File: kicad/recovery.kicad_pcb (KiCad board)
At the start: 2 copper layers, 84.1 x 61.7 mm, 50 parts, among them J1 Bus_PCI_Express_x1, J2 wago 2060-452/998-404, J3 wago 2060-452/998-404, J4 Conn_01x04, J5 Conn_01x02_Pin, J6 USB_C_Receptacle_USB2.0_16P, Q1 SI7232DN-T1-GE3, U2 RP2040, U4 W25Q128JVP, U9 MCP25625T-E/ML, X1 RP2040 Crystal, Y2 X322516MLB4SI

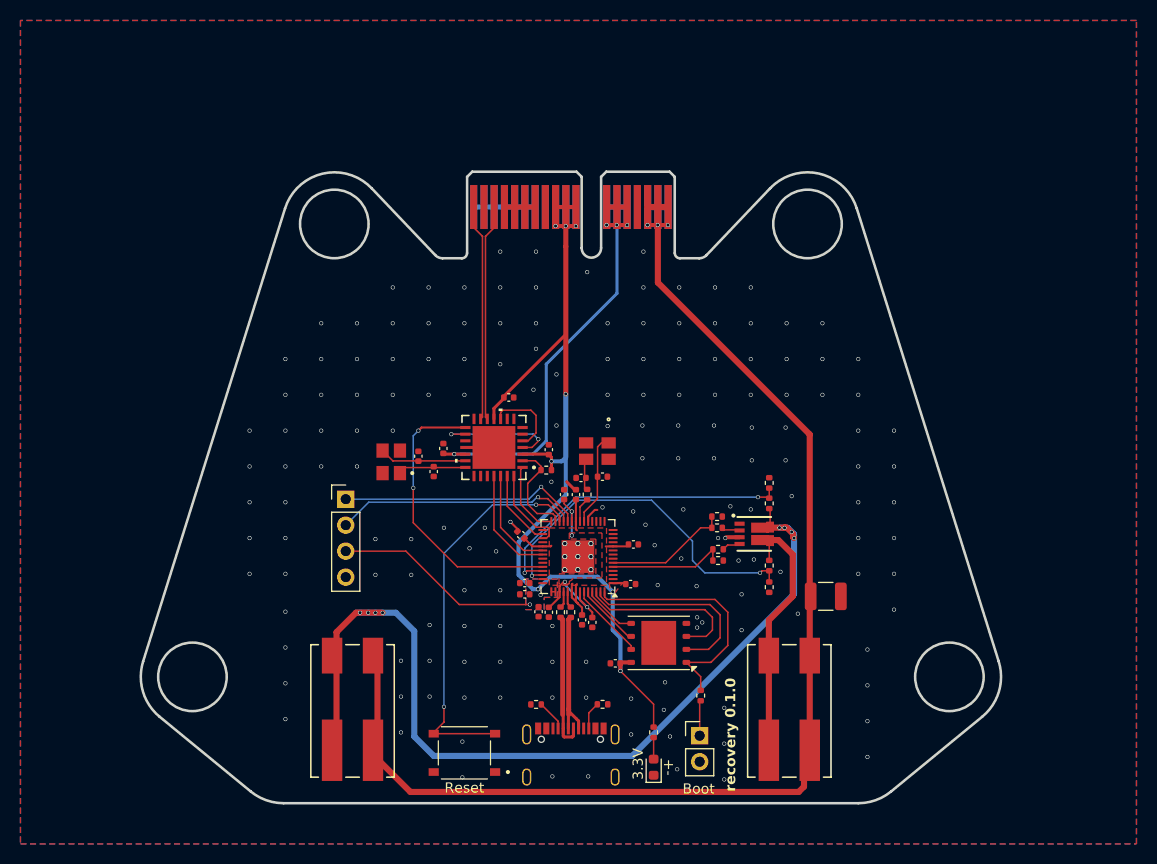
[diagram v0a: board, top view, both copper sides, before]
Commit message: feat: overhauled recovery board: added servos, solenoids, PWM-level shifters and firing circuit to layout
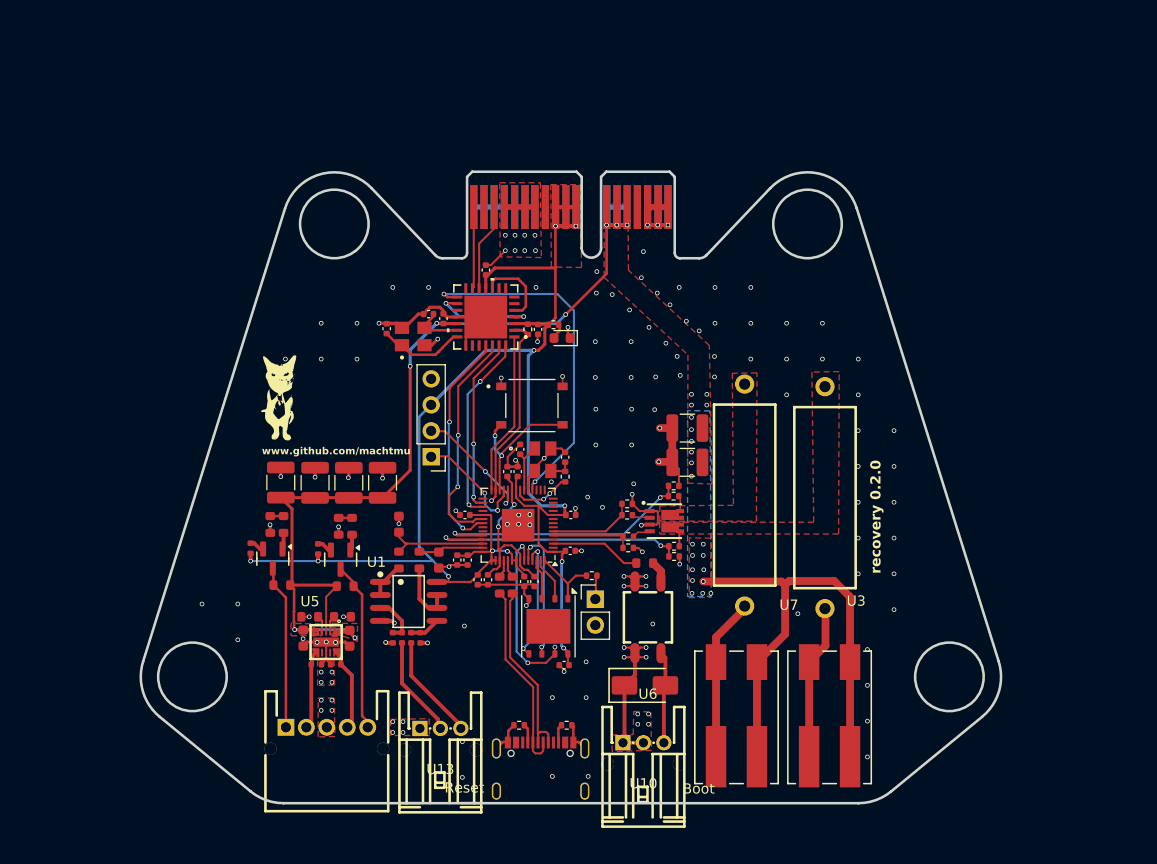
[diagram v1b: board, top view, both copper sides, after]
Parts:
- removed R203, R204: 27, Resistor_SMD:R_0402_1005Metric
- added C2: 100pF, PCM_JLCPCB:C_0603, F.Cu at (133.5, 98.7)
- added C21: 1uF, PCM_JLCPCB:C_0603, F.Cu at (120.2, 106.3)
- added C28: 1uF, PCM_JLCPCB:C_0603, F.Cu at (124.8, 106.3)
- added C29: 100nF, PCM_JLCPCB:C_0402, F.Cu at (123.4, 108.8)
- added C3: 100u, Capacitor_SMD:C_1210_3225Metric, F.Cu at (157.8, 89.1)
- added C30: 100nF, PCM_JLCPCB:C_0402, F.Cu at (121.5, 108.8)
- added C4: 100pF, PCM_JLCPCB:C_0603, F.Cu at (129.6, 95.2)
- added C5: 100u, Capacitor_SMD:C_1210_3225Metric, F.Cu at (118.0, 91.1)
- added C6: 100u, Capacitor_SMD:C_1210_3225Metric, F.Cu at (121.4, 91.1)
- added C7: 100u, Capacitor_SMD:C_1210_3225Metric, F.Cu at (128.0, 91.1)
- added C8: 100u, Capacitor_SMD:C_1210_3225Metric, F.Cu at (124.7, 91.1)
- added D2: SS210, PCM_JLCPCB:D_SMA, F.Cu at (153.7, 110.9)
- added G***: LOGO, LOGO, F.Cu at (117.8, 82.8)
- added Q2: AO3400A, PCM_JLCPCB:Q_SOT-23, F.Cu at (123.9, 98.6)
- added Q3: AO3400A, PCM_JLCPCB:Q_SOT-23, F.Cu at (117.3, 98.5)
- added R1: 100Ω, PCM_JLCPCB:R_0603, F.Cu at (131.6, 98.7)
- added R10: 300Ω, PCM_JLCPCB:R_0603, F.Cu at (153.6, 99.0)
- added R11: 27Ω, PCM_JLCPCB:R_0603, F.Cu at (139.4, 101.1)
- added R13: 5.1kΩ, PCM_JLCPCB:R_0603, F.Cu at (124.1, 104.2)
- added R14: 5.1kΩ, PCM_JLCPCB:R_0603, F.Cu at (120.9, 104.2)
- added R15: 120Ω, PCM_JLCPCB:R_0603, F.Cu at (125.0, 95.3)
- added R16: 5.1kΩ, PCM_JLCPCB:R_0603, F.Cu at (123.7, 95.3)
- added R17: 5.1kΩ, PCM_JLCPCB:R_0603, F.Cu at (117.0, 95.2)
- added R18: 120Ω, PCM_JLCPCB:R_0603, F.Cu at (118.3, 95.2)
- added R19: 5.1kΩ, PCM_JLCPCB:R_0603, F.Cu at (118.2, 101.1)
- added R24: 5.1kΩ, PCM_JLCPCB:R_0603, F.Cu at (124.3, 101.2)
- added R25: 10kΩ, PCM_JLCPCB:R_0402, F.Cu at (121.7, 97.6)
- added R26: 10kΩ, PCM_JLCPCB:R_0402, F.Cu at (115.1, 97.5)
- added R35: 27Ω, PCM_JLCPCB:R_0603, F.Cu at (140.7, 101.1)
- added R36: 100Ω, PCM_JLCPCB:R_0603, F.Cu at (129.6, 98.7)
- added R5: 100kΩ, PCM_JLCPCB:R_0402, F.Cu at (129.9, 106.2)
- added R6: 33kΩ, PCM_JLCPCB:R_0402, F.Cu at (129.0, 106.2)
- added R7: 100kΩ, PCM_JLCPCB:R_0402, F.Cu at (130.8, 106.2)
- added R8: 33kΩ, PCM_JLCPCB:R_0402, F.Cu at (131.7, 106.2)
- added U1: MCP6002T-I/SN, easyeda2kicad:SOIC-8_L4.9-W3.9-P1.27-LS6.0-BL, F.Cu at (130.6, 102.7)
- added U10: S03B-PASK-2, easyeda2kicad:CONN-TH_S03B-PASK-2-LF-SN, F.Cu at (153.5, 116.5)
- added U13: S03B-PASK-2, easyeda2kicad:CONN-TH_S03B-PASK-2-LF-SN, F.Cu at (133.7, 115.1)
- added U3: MOF5WS-5.1Ω±5% T, easyeda2kicad:RES-TH_BD6.0-L17.5-P21.50-D0.7, F.Cu at (171.2, 92.5)
- added U5: TPS22976DPUR, easyeda2kicad:WSON-14_L3.0-W2.0-P0.40-BL-EP-1, F.Cu at (122.5, 106.7)
- added U6: GAQY252G3S, easyeda2kicad:SOP-4_L4.3-W4.4-P2.54-LS7.0-BL, F.Cu at (153.9, 104.2)
- added U7: MOF5WS-5.1Ω±5% T, easyeda2kicad:RES-TH_BD6.0-L17.5-P21.50-D0.7, F.Cu at (163.4, 92.3)
- added U8: S05B-PASK-2(LF)(SN), easyeda2kicad:CONN-TH_S05B-PASK-2-LF-SN, F.Cu at (122.5, 115.0)
- moved D1 42.9 mm to (145.6, 77.0), turned to 180 degrees
- moved R2 41.0 mm to (144.7, 75.7), turned to 0 degrees
- moved J2 37.5 mm to (162.6, 114.0)
- moved S2 34.6 mm to (142.6, 83.5), turned to 0 degrees
- moved C1 21.3 mm to (157.8, 85.8), turned to 180 degrees
- moved J5 16.8 mm to (148.8, 102.5)
- moved R30 15.8 mm to (148.4, 100.2), turned to 0 degrees
- moved C94 14.7 mm to (128.4, 76.0), turned to 90 degrees
- moved C95 13.9 mm to (132.5, 74.6), turned to 180 degrees
- moved R91 13.9 mm to (142.2, 76.1), turned to -90 degrees
- moved U9 12.8 mm to (138.1, 74.9)
- moved C93 12.7 mm to (133.9, 75.0)
- moved C90 12.7 mm to (138.1, 70.3), turned to 90 degrees
- moved Y2 12.4 mm to (131.0, 76.8), turned to 90 degrees
- moved C92 11.8 mm to (143.2, 76.1), turned to -90 degrees
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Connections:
- C1 pad 1: v_lipo -> +5V
- J2 pad 3: v_lipo -> +5V
- J2 pad 4: v_lipo -> +5V
- J3 pad 3: v_lipo -> +5V
- J3 pad 4: v_lipo -> +5V
- J4 pad 1: /SWCLK -> /SWD
- J4 pad 2: /SWD -> /SWCLK
- Q1 pad 5: Net-(J3-1_1) -> Net-(Q1-Pad5)
- Q1 pad 6: Net-(J3-1_1) -> Net-(Q1-Pad5)
- Q1 pad 7: Net-(J2-1_1) -> Net-(Q1-Pad7)
- Q1 pad 8: Net-(J2-1_1) -> Net-(Q1-Pad7)
- R22 pad 2: Net-(J3-1_1) -> Net-(Q1-Pad5)
- R32 pad 2: Net-(J2-1_1) -> Net-(Q1-Pad7)
- U2 pad 18: unconnected-(U2-GPIO15-Pad18) -> CANSTBY
- U2 pad 3: unconnected-(U2-GPIO1-Pad3) -> /MCU_SOLENOID
- U2 pad 38: CANSTBY -> sense_m
- U2 pad 39: sense_m -> sense_d
- U2 pad 40: sense_d -> /PT_1
- U2 pad 41: unconnected-(U2-GPIO29_ADC3-Pad41) -> /PT_2
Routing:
- net v_lipo: track 119.1 -> 6.00 mm
- net GND: track 17.7 -> 122.7 mm, vias 178 -> 152
- net +5V: track 43.2 -> 141.3 mm, vias 4 -> 29
- net Net-(J2-1_1): track 92.3 -> 15.9 mm, vias 8 -> 0
- net /RUN: track 38.3 -> 14.4 mm
- net +3.3V: track 132.6 -> 151.7 mm, vias 10 -> 11
- net /5V_PWM1: track 0.00 -> 16.7 mm
- net /5V_PWM2: track 0.00 -> 16.2 mm
- net /QSPI_SS: track 24.5 -> 8.31 mm
- net /QSPI_SD1: track 18.9 -> 4.32 mm
- net CANH: track 21.1 -> 8.01 mm
- net /SWD: track 23.8 -> 11.1 mm, vias 1 -> 2
- net /QSPI_SD2: track 16.7 -> 3.96 mm
- net CANL: track 21.1 -> 8.57 mm
- net /SWCLK: track 24.0 -> 11.9 mm, vias 1 -> 2
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- added copper zone on B.Cu, net +5V
- added copper zone on F.Cu, net +5V
- added copper zone on In1.Cu, net GND
- added copper zone on In2.Cu, net GND
- added copper zone on F.Cu, net Net-(Q1-Pad5)
- added copper zone on F.Cu, net Net-(Q1-Pad7)
- removed copper zone on F.Cu, net +1V1
- removed copper zone on B.Cu, net +3.3V
- removed copper zone on B.Cu, net GND
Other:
- copper layers 2 -> 4
- board text added: "recovery 0.2.0"
- board text added: "www.github.com/machtmu"
- board text removed: "+-"
- board text removed: "3.3V"
- board text removed: "recovery 0.1.0"

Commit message: Feat: Completed layout, modified divider network for 5V PT operation
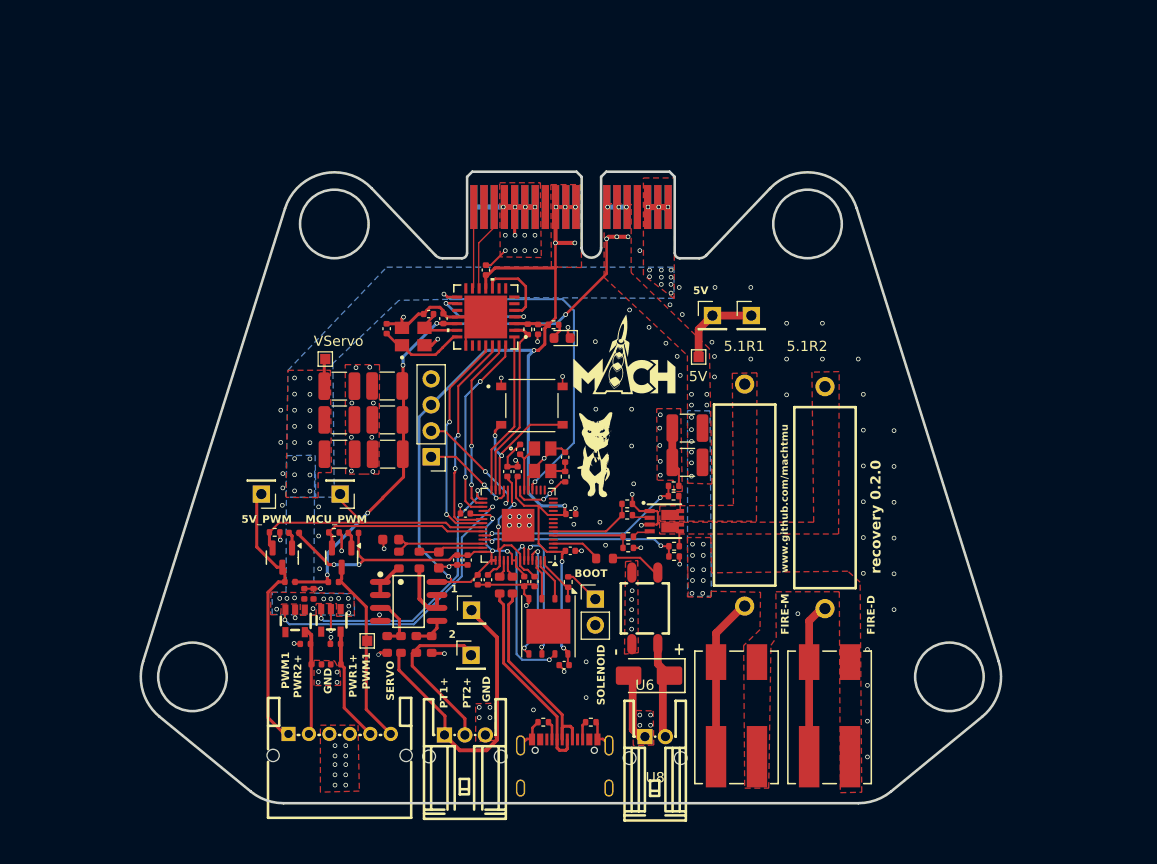
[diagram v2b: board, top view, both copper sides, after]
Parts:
- removed C21, C28: 1uF, PCM_JLCPCB:C_0603
- removed R19, R24: 5.1kΩ, PCM_JLCPCB:R_0603
- removed R25: 10kΩ, PCM_JLCPCB:R_0402
- removed R6, R8: 33kΩ, PCM_JLCPCB:R_0402
- removed U10: S03B-PASK-2, easyeda2kicad:CONN-TH_S03B-PASK-2-LF-SN
- added 5V: TestPoint_Pad_1.0x1.0mm, TestPoint:TestPoint_Pad_1.0x1.0mm, F.Cu at (158.9, 78.8)
- added C12: 100u, Capacitor_SMD:C_1210_3225Metric, F.Cu at (123.8, 85.0)
- added C12: 100u, Capacitor_SMD:C_1210_3225Metric, F.Cu at (123.8, 88.3)
- added C13: 100u, Capacitor_SMD:C_1210_3225Metric, F.Cu at (123.8, 81.7)
- added C5: 1uF, PCM_JLCPCB:C_0402, F.Cu at (120.3, 102.0)
- added C5: 100u, Capacitor_SMD:C_1210_3225Metric, F.Cu at (128.5, 88.3)
- added C6: 1uF, PCM_JLCPCB:C_0402, F.Cu at (121.2, 102.0)
- added CN1: S06B-PASK-2(LF)(SN), easyeda2kicad:CONN-TH_6P-P2.00_S06B-PASK-2-LF-SN, F.Cu at (123.8, 115.7)
- added G***: LOGO, LOGO, F.Cu at (151.7, 79.5)
- added PWM1: TestPoint_Pad_1.0x1.0mm, TestPoint:TestPoint_Pad_1.0x1.0mm, F.Cu at (126.5, 106.5)
- added R9: 10kΩ, PCM_JLCPCB:R_0402, F.Cu at (125.2, 96.0)
- added REF**: PinHeader_1x01_P2.54mm_Vertical, Connector_PinHeader_2.54mm:PinHeader_1x01_P2.54mm_Vertical, F.Cu at (164.1, 74.8)
- added REF**: PinHeader_1x01_P2.54mm_Vertical, Connector_PinHeader_2.54mm:PinHeader_1x01_P2.54mm_Vertical, F.Cu at (136.7, 103.5)
- added REF**: PinHeader_1x01_P2.54mm_Vertical, Connector_PinHeader_2.54mm:PinHeader_1x01_P2.54mm_Vertical, F.Cu at (160.2, 74.8)
- added REF**: PinHeader_1x01_P2.54mm_Vertical, Connector_PinHeader_2.54mm:PinHeader_1x01_P2.54mm_Vertical, F.Cu at (123.8, 92.2)
- added REF**: PinHeader_1x01_P2.54mm_Vertical, Connector_PinHeader_2.54mm:PinHeader_1x01_P2.54mm_Vertical, F.Cu at (136.7, 108.0)
- added REF**: PinHeader_1x01_P2.54mm_Vertical, Connector_PinHeader_2.54mm:PinHeader_1x01_P2.54mm_Vertical, F.Cu at (116.2, 92.2)
- added U11: TMI6240, easyeda2kicad:SOT-23-5_L2.9-W1.6-P0.95-LS2.8-BL, F.Cu at (123.0, 104.5)
- added VServo: TestPoint_Pad_1.0x1.0mm, TestPoint:TestPoint_Pad_1.0x1.0mm, F.Cu at (122.4, 79.0)
- C7, C8: value 100u -> 1uF; footprint Capacitor_SMD:C_1210_3225Metric -> PCM_JLCPCB:C_0402
- R13, R14: value 5.1kΩ -> 10kΩ; footprint PCM_JLCPCB:R_0603 -> PCM_JLCPCB:R_0402
- R15: value 120Ω -> 1k; footprint PCM_JLCPCB:R_0603 -> Resistor_SMD:R_0402_1005Metric
- R16: value 5.1kΩ -> 1k; footprint PCM_JLCPCB:R_0603 -> Resistor_SMD:R_0402_1005Metric
- R17: value 5.1kΩ -> 33kΩ
- R18: value 120Ω -> 100kΩ
- R5, R7: value 100kΩ -> 51kΩ; footprint PCM_JLCPCB:R_0402 -> PCM_JLCPCB:R_0603
- U5: value TPS22976DPUR -> TMI6240; footprint easyeda2kicad:WSON-14_L3.0-W2.0-P0.40-BL-EP-1 -> easyeda2kicad:SOT-23-5_L2.9-W1.6-P0.95-LS2.8-BL
- U8: value S05B-PASK-2(LF)(SN) -> S02B-PASK-2(LF)(SN); footprint easyeda2kicad:CONN-TH_S05B-PASK-2-LF-SN -> easyeda2kicad:CONN-TH_S02B-PASK-2-LF-SN
- moved U8 32.1 mm to (154.7, 115.9), turned to 180 degrees
- moved G*** 31.4 mm to (148.8, 88.3)
- moved R17 19.7 mm to (132.8, 106.9), turned to -90 degrees
- moved C7 17.5 mm to (120.5, 106.8), turned to 0 degrees
- moved C8 15.8 mm to (123.4, 106.8), turned to 0 degrees
- moved R18 15.5 mm to (128.4, 106.9)
- moved C5 12.1 mm to (128.5, 85.0), turned to 180 degrees
- moved C6 11.8 mm to (128.4, 81.6), turned to 180 degrees
- moved R16 6.29 mm to (117.5, 95.9), turned to 180 degrees
- moved R26 4.51 mm to (119.3, 96.0), turned to 0 degrees
- moved R10 3.95 mm to (149.7, 98.5)
- moved R14 3.92 mm to (119.0, 100.8)
- moved U5 3.67 mm to (119.5, 104.6)
- moved R13 3.51 mm to (123.2, 100.8)
- moved U13 2.48 mm to (136.1, 115.8)
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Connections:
- net CANH renamed /CANP
- net CANL renamed /CANN
- C7 pad 1: +5V -> GND
- C7 pad 2: GND -> /SERVO_PWR2
- C8 pad 1: +5V -> GND
- C8 pad 2: GND -> /SERVO_PWR1
- D2 pad 1: GND -> +24V
- D2 pad 2: +24V -> GND
- J1 pad A16: v_lipo -> v_servo
- J1 pad A17: v_lipo -> v_servo
- J1 pad A18: v_lipo -> v_servo
- J1 pad B16: v_lipo -> v_servo
- J1 pad B17: v_lipo -> v_servo
- J1 pad B18: v_lipo -> v_servo
- Q2 pad 2: /3.3V_PWM1 -> /MCU_PWM1
- Q3 pad 2: /3.3V_PWM2 -> /MCU_PWM2
- R13 pad 1: GND -> /5V_PWM1
- R13 pad 2: /SERVO_ON1 -> +5V
- R14 pad 1: GND -> /5V_PWM2
- R14 pad 2: /SERVO_ON2 -> +5V
- R15 pad 1: /MCU_PWM1 -> GND
- R15 pad 2: Net-(Q2-G) -> /MCU_PWM1
- R16 pad 2: /MCU_PWM1 -> /MCU_PWM2
- R17 pad 1: GND -> Net-(U1-+INB)
- R17 pad 2: /MCU_PWM2 -> GND
- R18 pad 1: /MCU_PWM2 -> Net-(U1-+INA)
- R18 pad 2: Net-(Q3-G) -> GND
- R26 pad 1: /3.3V_PWM2 -> Net-(Q3-G)
- R5 pad 1: /PT_IN1 -> /PT_IN2
- R5 pad 2: Net-(U1-+INA) -> Net-(U1-+INB)
- R7 pad 1: /PT_IN2 -> /PT_IN1
- R7 pad 2: Net-(U1-+INB) -> Net-(U1-+INA)
- U13 pad 1: GND -> /PT_IN1
- U13 pad 2: /PT_IN1 -> /PT_IN2
- U13 pad 3: /PT_IN2 -> GND
- U2 pad 29: unconnected-(U2-GPIO18-Pad29) -> /SERVO_ON1
- U2 pad 32: unconnected-(U2-GPIO21-Pad32) -> /SERVO_ON2
- U2 pad 36: unconnected-(U2-GPIO24-Pad36) -> /MCU_PWM2
- U2 pad 37: unconnected-(U2-GPIO25-Pad37) -> /MCU_PWM1
- U5 pad 1: +5V -> v_servo
- U5 pad 2: +5V -> GND
- U5 pad 3: /SERVO_ON1 -> /SERVO_ON2
- U5 pad 4: +5V -> unconnected-(U5-SS-Pad4)
- U5 pad 5: /SERVO_ON2 -> /SERVO_PWR2
- U8 pad 1: /5V_PWM2 -> GND
- U8 pad 2: /SERVO_PWR2 -> +24V
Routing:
- net +5V: track 141.3 -> 69.0 mm, vias 29 -> 31
- net /SERVO_ON1: track 1.61 -> 30.2 mm, vias 0 -> 2
- net /SERVO_ON2: track 1.61 -> 29.6 mm, vias 0 -> 2
- net /MCU_PWM2: track 1.30 -> 26.8 mm
- net GND: track 122.7 -> 99.8 mm, vias 152 -> 145
- net /PT_IN1: track 9.71 -> 28.9 mm
- net /MCU_PWM1: track 1.30 -> 17.2 mm
- net /5V_PWM2: track 16.2 -> 27.0 mm
- net sense_d: track 26.8 -> 19.6 mm
- net v_servo: track 0.00 -> 6.66 mm, vias 0 -> 39
- net /PT_IN2: track 10.2 -> 16.5 mm
- net v_lipo: track 6.00 -> 0.00 mm, vias 3 -> 0
- net sense_m: track 26.3 -> 20.7 mm
- net /MCU_SOLENOID: track 8.90 -> 4.99 mm
- net /QSPI_SS: track 8.31 -> 4.68 mm
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- added copper zone on B.Cu, net v_servo
- added copper zone on F.Cu, net v_servo
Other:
- board text added: "+"
- board text added: "-"
- board text added: "1"
- board text added: "100k"
- board text added: "2"
- board text added: "33k"
- board text added: "5.1R1"
- board text added: "5.1R2"
- board text added: "5V"
- board text added: "5V_PWM"
- board text added: "BOOT"
- board text added: "FIRE-D"
- board text added: "FIRE-M"
- board text added: "GND"
- board text added: "MCU_PWM"
- board text added: "PT1+"
- board text added: "PT2+"
- board text added: "PWM1"
- board text added: "PWR1+"
- board text added: "PWR2+"
- board text added: "SERVO"
- board text added: "SOLENOID"
- board text removed: "Boot"
- board text removed: "Reset"
